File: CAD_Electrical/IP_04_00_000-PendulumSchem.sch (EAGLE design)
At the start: 7 parts

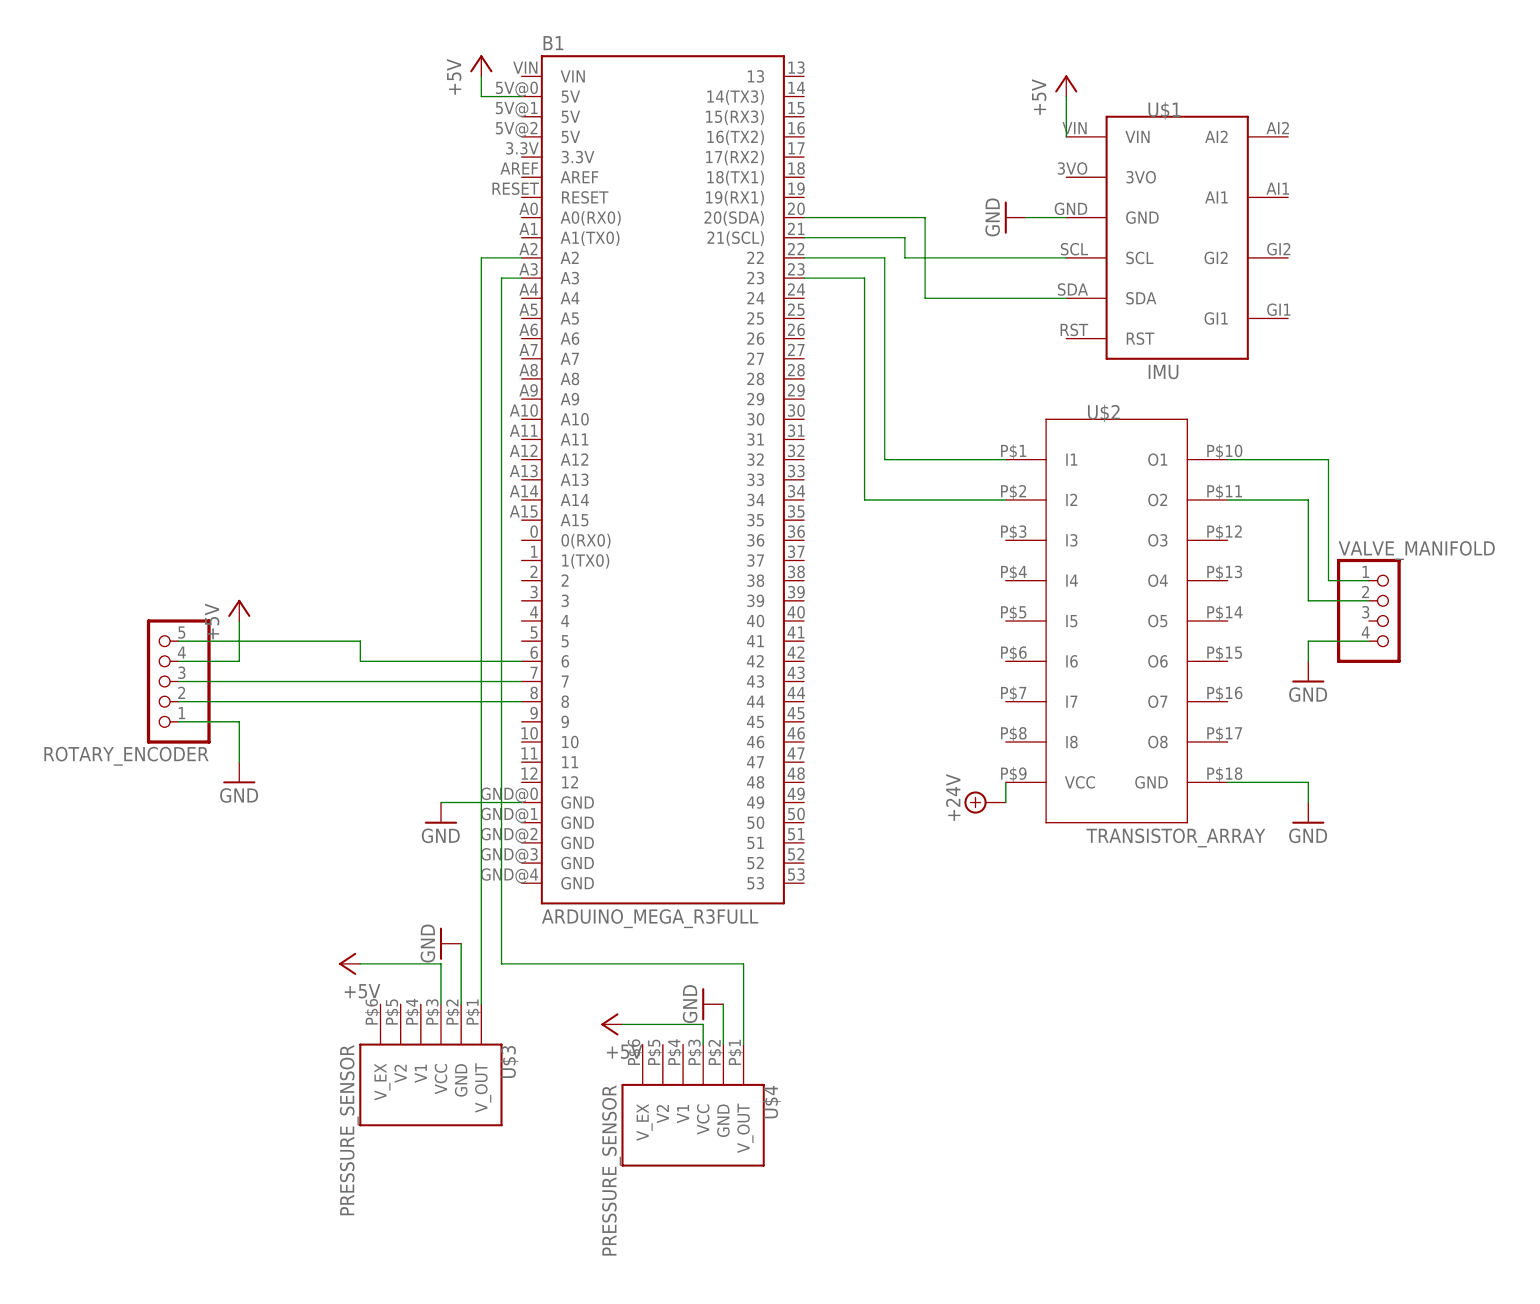
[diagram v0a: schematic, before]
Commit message: Fixed encoder routing to interrupt & created ground plane
Also inserted text, fixed footprints of custom devices, and replaced standard pins with screw terminals for more secure connection
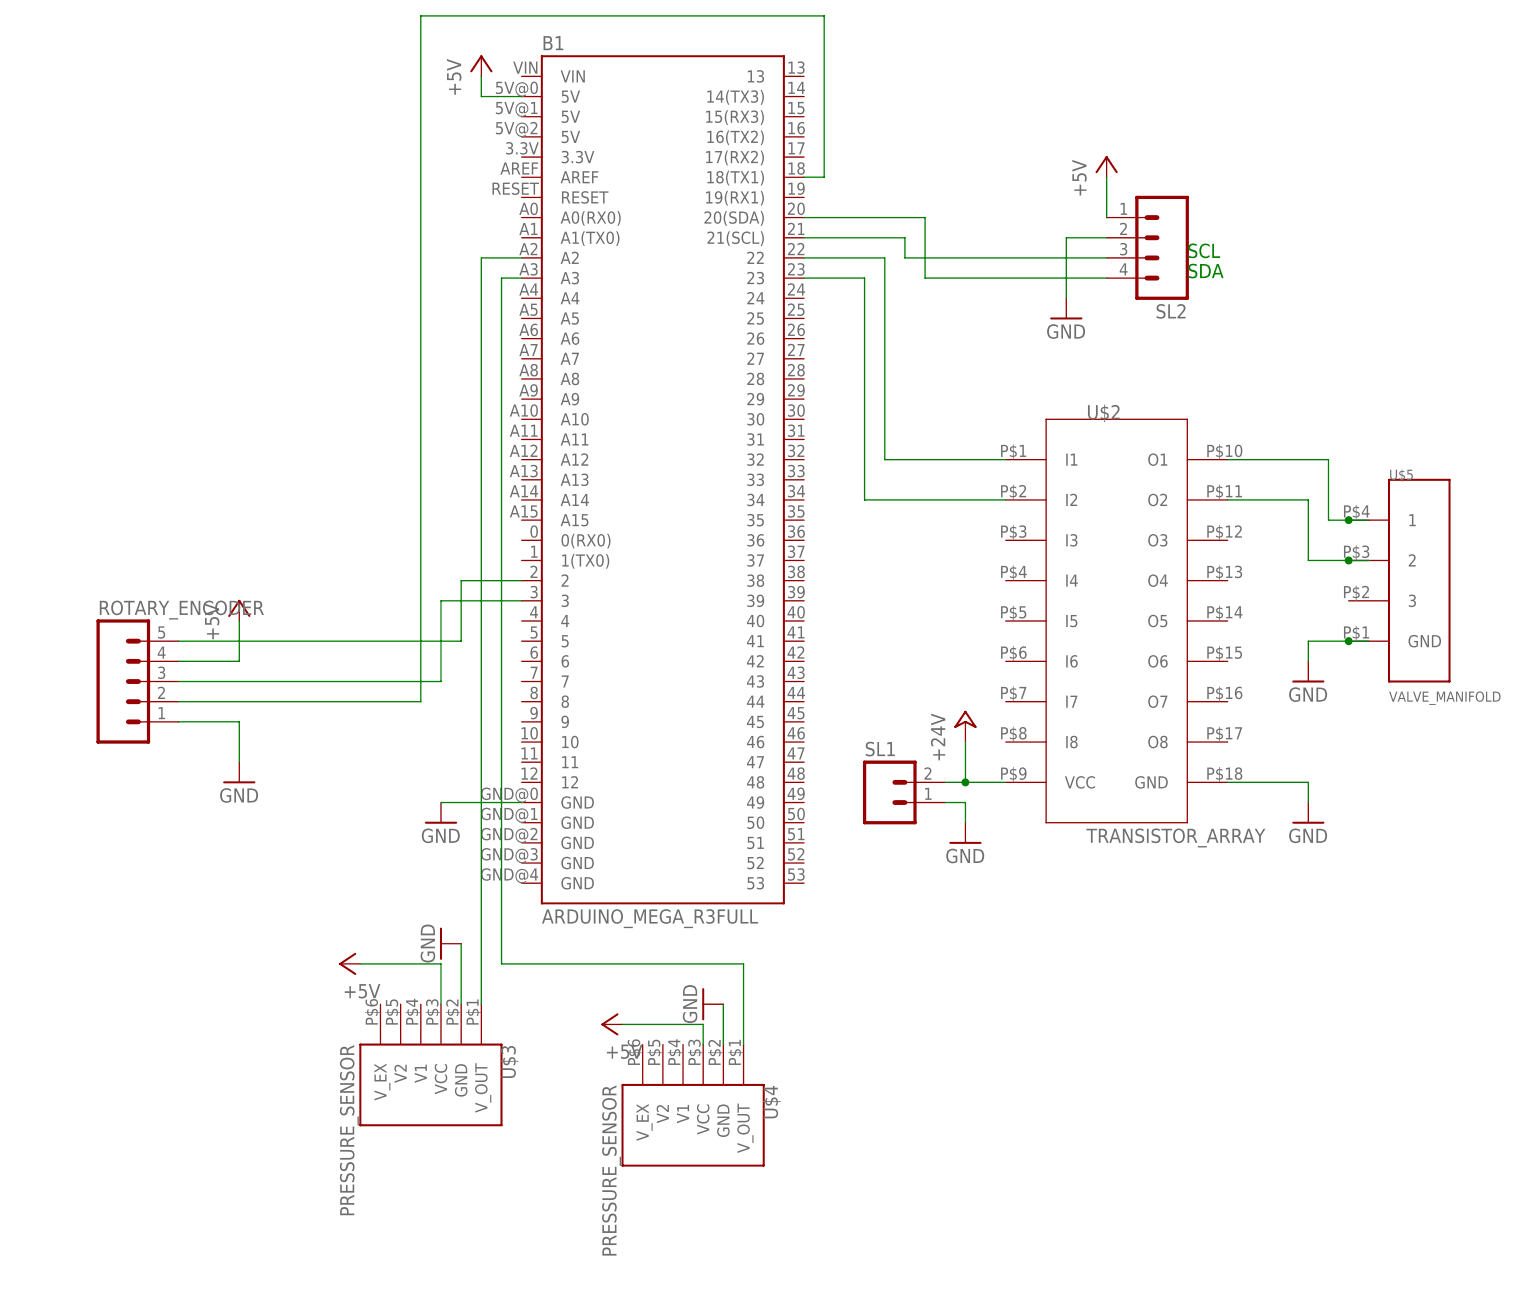
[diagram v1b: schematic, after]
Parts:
- removed U$1: IMU, IPcustomDevices:IMU
- removed VALVE_MANIFOLD: (no value), pinhead:PINHD-1X4
- added SL1: (no value), con-amp-quick:M02
- added SL2: (no value), con-amp-quick:M04
- added U$5: VALVE_MANIFOLD, IPcustomDevices:VALVE_MANIFOLD
- ROTARY_ENCODER: device pinhead:PINHD-1X5 -> con-amp-quick:M05
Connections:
- removed net N$11: B1.8, ROTARY_ENCODER.2
- removed net N$9: B1.6, ROTARY_ENCODER.5
- new net N$2: B1.20(SDA), SL2.4
- new net N$4: B1.2, ROTARY_ENCODER.5
- net +24V: now also SL1.2
- net +5V: now also SL2.1; no longer U$1.VIN
- net GND: now also SL1.1, SL2.2, U$5.GND; no longer U$1.GND, VALVE_MANIFOLD.4
- net N$1: now also B1.3; no longer B1.7
- net N$3: now also B1.21(SCL), SL2.3; no longer B1.20(SDA), U$1.SDA
- net N$6: now also U$5.1; no longer VALVE_MANIFOLD.1
- net N$7: now also B1.18(TX1), ROTARY_ENCODER.2; no longer B1.21(SCL), U$1.SCL
- net N$8: now also U$5.2; no longer VALVE_MANIFOLD.2
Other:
- note added: "SCL"
- note added: "SDA"

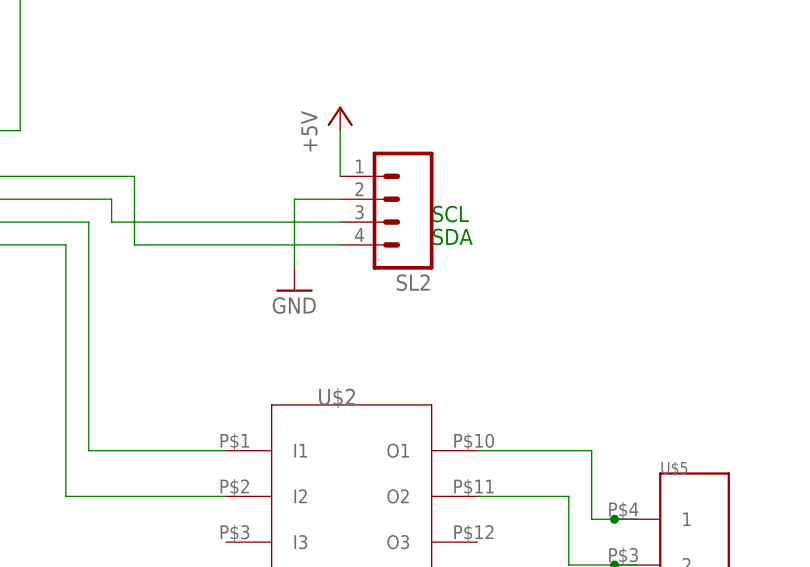
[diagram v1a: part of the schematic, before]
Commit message: Updated silkscreen to only part names plus external wires
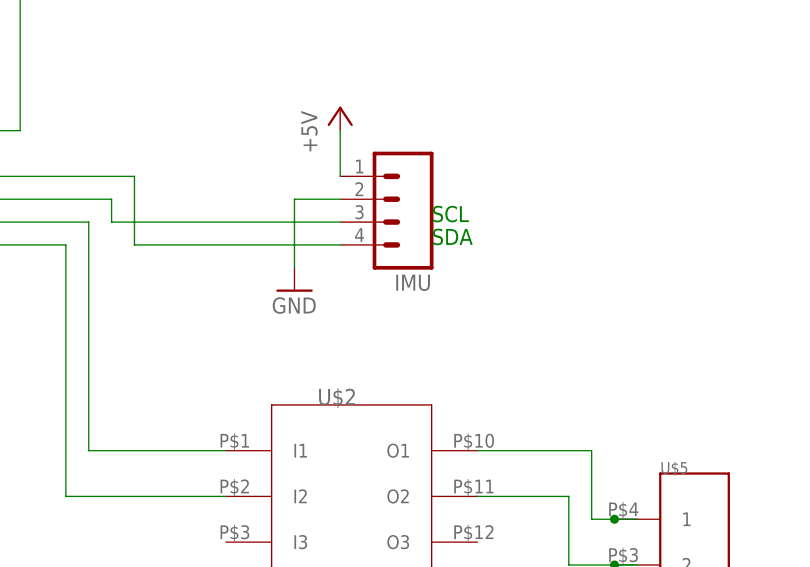
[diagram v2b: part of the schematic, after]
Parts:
- renumbered SL2 to IMU
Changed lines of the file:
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@@
 <part name="SL1" library="con-amp-quick" library_urn="urn:adsk.eagle:library:125" deviceset="M02" device="" package3d_urn="urn:adsk.eagle:package:5956/1"/>
 <part name="ROTARY_ENCODER" library="con-amp-quick" library_urn="urn:adsk.eagle:library:125" deviceset="M05" device="" package3d_urn="urn:adsk.eagle:package:5961/1"/>
-<part name="SL2" library="con-amp-quick" library_urn="urn:adsk.eagle:library:125" deviceset="M04" device="" package3d_urn="urn:adsk.eagle:package:5958/1"/>
+<part name="IMU" library="con-amp-quick" library_urn="urn:adsk.eagle:library:125" deviceset="M04" device="" package3d_urn="urn:adsk.eagle:package:5958/1"/>
 </parts>
 <sheets>
@@
 <attribute name="NAME" x="35.56" y="84.582" size="1.778" layer="95"/>
 </instance>
-<instance part="SL2" gate="G$1" x="167.64" y="132.08" smashed="yes" rot="R180">
+<instance part="IMU" gate="G$1" x="167.64" y="132.08" smashed="yes" rot="R180">
 <attribute name="VALUE" x="172.72" y="139.7" size="1.778" layer="96" rot="R180"/>
 <attribute name="NAME" x="172.72" y="123.698" size="1.778" layer="95" rot="R180"/>
@@
 <pinref part="GND3" gate="1" pin="GND"/>
 <wire x1="157.48" y1="132.08" x2="157.48" y2="124.46" width="0.1524" layer="91"/>
-<pinref part="SL2" gate="G$1" pin="2"/>
+<pinref part="IMU" gate="G$1" pin="2"/>
 <wire x1="157.48" y1="132.08" x2="162.56" y2="132.08" width="0.1524" layer="91"/>
 </segment>
@@
 <segment>
 <pinref part="P+1" gate="1" pin="+5V"/>
-<pinref part="SL2" gate="G$1" pin="1"/>
+<pinref part="IMU" gate="G$1" pin="1"/>
 <wire x1="162.56" y1="139.7" x2="162.56" y2="134.62" width="0.1524" layer="91"/>
 </segment>
@@
 <wire x1="124.46" y1="134.62" x2="139.7" y2="134.62" width="0.1524" layer="91"/>
 <wire x1="139.7" y1="134.62" x2="139.7" y2="127" width="0.1524" layer="91"/>
-<pinref part="SL2" gate="G$1" pin="4"/>
+<pinref part="IMU" gate="G$1" pin="4"/>
 <wire x1="139.7" y1="127" x2="162.56" y2="127" width="0.1524" layer="91"/>
 </segment>
@@
 <wire x1="124.46" y1="132.08" x2="137.16" y2="132.08" width="0.1524" layer="91"/>
 <wire x1="137.16" y1="132.08" x2="137.16" y2="129.54" width="0.1524" layer="91"/>
-<pinref part="SL2" gate="G$1" pin="3"/>
+<pinref part="IMU" gate="G$1" pin="3"/>
 <wire x1="137.16" y1="129.54" x2="162.56" y2="129.54" width="0.1524" layer="91"/>
 </segment>

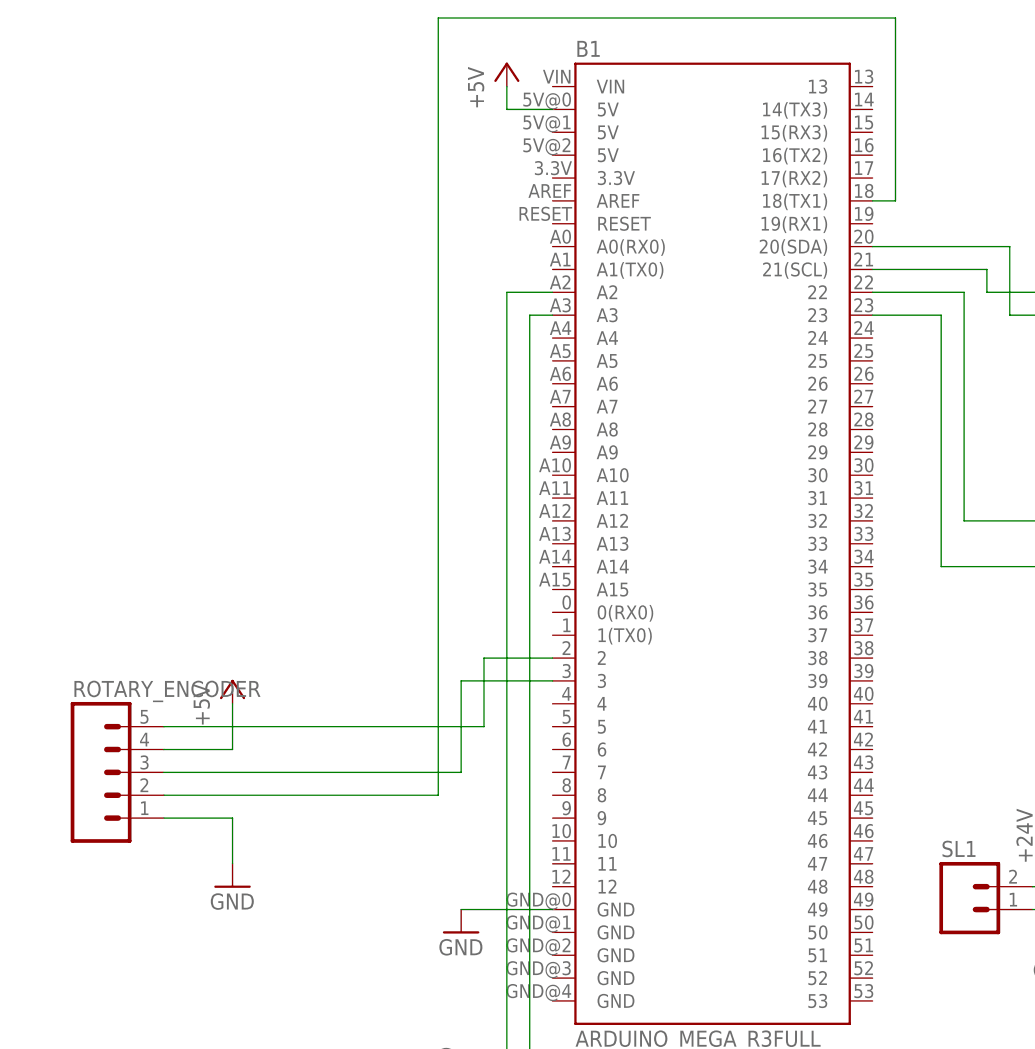
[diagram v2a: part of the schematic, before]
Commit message: Widened 24V connection & Deleted extraneous holes & MicroSD added
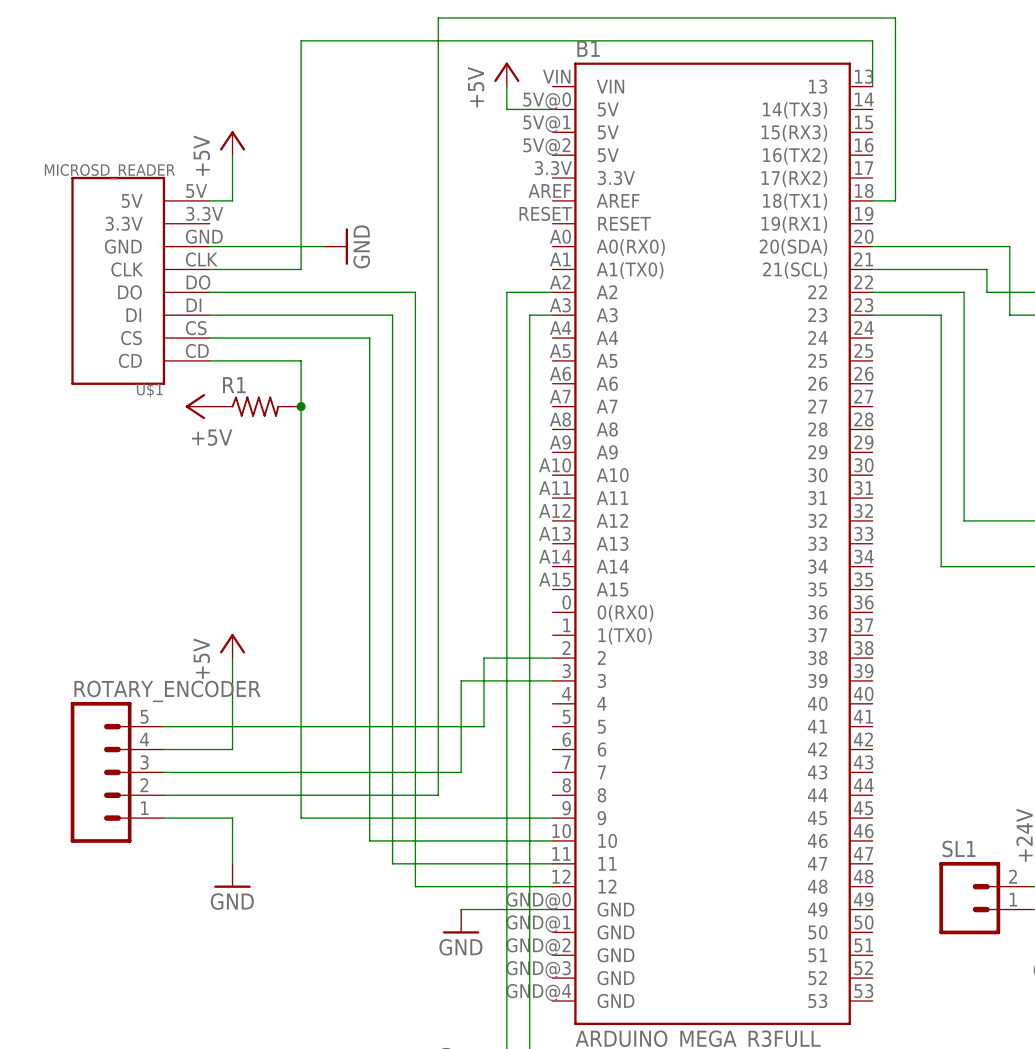
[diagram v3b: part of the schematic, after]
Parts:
- added R1: (no value), rcl:R-US_0204/7
- added U$1: MICROSD_READER, IPcustomDevices:MICROSD_READER
- B1: device SparkFun-Boards:ARDUINO_MEGA_R3FULL -> SparkFun-Boards-deleted2holes:ARDUINO_MEGA_R3FULL
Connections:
- new net N$11: B1.13, U$1.CLK
- new net N$13: B1.12, U$1.DO
- new net N$15: B1.11, U$1.DI
- new net N$16: B1.10, U$1.CS
- new net N$18: B1.9, R1.2, U$1.CD
- net +5V: now also R1.1, U$1.5V
- net GND: now also U$1.GND
